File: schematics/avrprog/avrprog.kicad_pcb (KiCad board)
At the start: 2 copper layers, 74.9 x 38.1 mm, 37 parts, among them J1 USB_B, J2 AVR-ISP-10, J3 PROG_PWR, J4 EMCLK, J5 SELF_PROG, U1 FT232RL, U2 ATmega8A-P, Y1 16MHz

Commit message: schematic ...
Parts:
- D8: value PPWRLED -> PWRLED
- moved R10 77.1 mm to (92.7, 57.1), turned to -90 degrees
- moved D7 69.5 mm to (99.4, 67.8), turned to 180 degrees
- moved R11 44.4 mm to (54.6, 87.6), turned to 90 degrees
- moved C1 9.89 mm to (53.3, 67.3)
- moved D8 9.04 mm to (38.1, 74.9), turned to -90 degrees
- moved C4 1.54 mm to (38.2, 69.6)
- moved FB1 1.00 mm to (48.0, 67.3)
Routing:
- net VCC: track 0.00 -> 44.2 mm, vias 0 -> 1
- net GND: track 0.00 -> 38.5 mm
- net Net-(D8-Pad2): track 0.00 -> 20.4 mm
- net Net-(FB1-Pad1): track 0.00 -> 14.0 mm, vias 0 -> 1
- net Net-(D2-Pad1): track 0.00 -> 13.2 mm
- net Net-(D1-Pad1): track 0.00 -> 9.94 mm
- net /RXLED#: track 0.00 -> 7.62 mm
- net /USB_D-: track 0.00 -> 5.08 mm
- net /USB_D+: track 0.00 -> 5.08 mm
- net Net-(C2-Pad2): track 0.00 -> 3.83 mm
- net /TXLED#: track 0.00 -> 3.81 mm
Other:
- board size 74.9 x 38.1 mm -> 76.2 x 38.1 mm

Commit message: schematic ...
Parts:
- added C10: 100nF, Capacitor_THT:C_Disc_D3.8mm_W2.6mm_P2.50mm, F.Cu at (54.6, 77.5)
- moved D8 70.4 mm to (96.5, 35.6)
- moved R11 66.6 mm to (88.9, 30.5), turned to -90 degrees
- moved D7 32.1 mm to (114.3, 39.4)
- moved R10 26.7 mm to (104.1, 33.0)
- moved J2 10.4 mm to (105.8, 67.3), turned to 180 degrees
- moved J5 3.81 mm to (69.8, 90.2)
- moved C4 2.17 mm to (38.2, 71.8)
- moved R7 1.28 mm to (97.8, 73.7)
- moved R8 1.28 mm to (102.9, 73.7)
- moved R9 1.28 mm to (107.9, 73.7)
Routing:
- net GND: track 38.5 -> 90.3 mm
- net VCC: track 44.2 -> 92.5 mm
- net /RXD_AT: track 0.00 -> 30.4 mm, vias 0 -> 1
- net Net-(D8-Pad2): track 20.4 -> 0.00 mm
- net /CTS_AT#: track 0.00 -> 16.0 mm, vias 0 -> 1
- net /RXD_FT232: track 0.00 -> 14.8 mm, vias 0 -> 1
- net /XTAL2_AT: track 0.00 -> 11.9 mm
- net /RESET_AT: track 0.00 -> 11.4 mm
- net /XTAL1_AT: track 0.00 -> 10.8 mm
- net /DTR_FT232#: track 0.00 -> 9.94 mm
- net Net-(D6-Pad2): track 0.00 -> 3.83 mm
- net Net-(D5-Pad2): track 0.00 -> 3.83 mm
- net Net-(D4-Pad2): track 0.00 -> 3.83 mm
- net /EMCLK_AT: track 0.00 -> 3.81 mm

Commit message: schematics completed
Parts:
- moved R11 45.8 mm to (91.4, 76.2), turned to 90 degrees
- moved R10 43.8 mm to (96.5, 76.2), turned to 90 degrees
- moved R6 36.9 mm to (58.4, 101.6)
- moved R4 35.1 mm to (76.2, 101.6)
- moved J5 34.7 mm to (55.9, 58.4)
- moved C1 27.9 mm to (27.9, 78.7), turned to -90 degrees
- moved D7 26.1 mm to (96.5, 58.4), turned to -90 degrees
- moved R5 24.4 mm to (58.4, 96.5)
- moved R9 24.3 mm to (91.4, 91.4), turned to 0 degrees
- moved D8 23.4 mm to (91.4, 58.4)
- moved FB1 20.8 mm to (27.9, 72.7), turned to -90 degrees
- moved J3 19.4 mm to (101.6, 76.2), turned to 180 degrees
- moved C4 17.6 mm to (53.3, 80.7), turned to 90 degrees
- moved R8 17.1 mm to (91.4, 86.4), turned to 0 degrees
- moved D2 16.3 mm to (48.3, 96.5), turned to 0 degrees
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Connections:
- net /RXD_AT renamed /TXD_FT232
- R5 pad 1: /CTS_AT# -> /RTS_FT232#
- U1 pad 11: /CTS_FT232# -> unconnected-(U1-Pad11)
- U1 pad 3: /CTS_AT# -> /RTS_FT232#
- U2 pad 4: /CTS_FT232# -> unconnected-(U2-Pad4)
- U2 pad 5: /CTS_AT# -> unconnected-(U2-Pad5)
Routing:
- net VCC: track 92.5 -> 0.00 mm, vias 1 -> 0
- net GND: track 90.3 -> 0.00 mm
- net /TXD_FT232: track 30.4 -> 0.00 mm, vias 1 -> 0
- net /CTS_AT#: track 16.0 -> 0.00 mm, vias 1 -> 0
- net /RXD_FT232: track 14.8 -> 0.00 mm, vias 1 -> 0
- net Net-(FB1-Pad1): track 14.0 -> 0.00 mm, vias 1 -> 0
- net Net-(D2-Pad1): track 13.2 -> 0.00 mm
- net /XTAL2_AT: track 11.9 -> 0.00 mm
- net /RESET_AT: track 11.4 -> 0.00 mm
- net /XTAL1_AT: track 10.8 -> 0.00 mm
- net Net-(D1-Pad1): track 9.94 -> 0.00 mm
- net /DTR_FT232#: track 9.94 -> 0.00 mm
- net /RXLED#: track 7.62 -> 0.00 mm
- net /USB_D-: track 5.08 -> 0.00 mm
- net /USB_D+: track 5.08 -> 0.00 mm
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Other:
- board size 76.2 x 38.1 mm -> 86.4 x 48.3 mm

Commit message: PCB finished
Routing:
- net GND: track 0.00 -> 198.4 mm, vias 0 -> 5
- net VCC: track 0.00 -> 155.2 mm, vias 0 -> 2
- net /RXD_FT232: track 0.00 -> 69.0 mm
- net /TXD_FT232: track 0.00 -> 57.3 mm, vias 0 -> 4
- net /RED_AT: track 0.00 -> 53.2 mm
- net /MISO_PRG: track 0.00 -> 35.7 mm, vias 0 -> 2
- net /DTR_FT232#: track 0.00 -> 35.5 mm, vias 0 -> 1
- net /SCK_PRG: track 0.00 -> 32.2 mm, vias 0 -> 2
- net /SCK_AT: track 0.00 -> 31.9 mm, vias 0 -> 1
- net /RESET_AT: track 0.00 -> 30.8 mm
- net /MOSI_PRG: track 0.00 -> 28.7 mm, vias 0 -> 2
- net /RST_PRG#: track 0.00 -> 27.6 mm, vias 0 -> 2
- net /YELLOW_AT: track 0.00 -> 27.0 mm
- net /TXLED#: track 0.00 -> 25.5 mm
- net /RXLED#: track 0.00 -> 23.9 mm, vias 0 -> 1
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
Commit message: crystal changed from 16MHz to 14.7456MHz due to USART communication
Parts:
- Y1: value 16MHz -> 14.7456MHz
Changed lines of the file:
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@@
       (effects (font (size 1 1) (thickness 0.15)))
     )
-    (fp_text value "16MHz" (at 2.44 3.525 90) (layer "F.Fab")
+    (fp_text value "14.7456MHz" (at 2.44 3.525 90) (layer "F.Fab")
       (effects (font (size 1 1) (thickness 0.15)))
     )

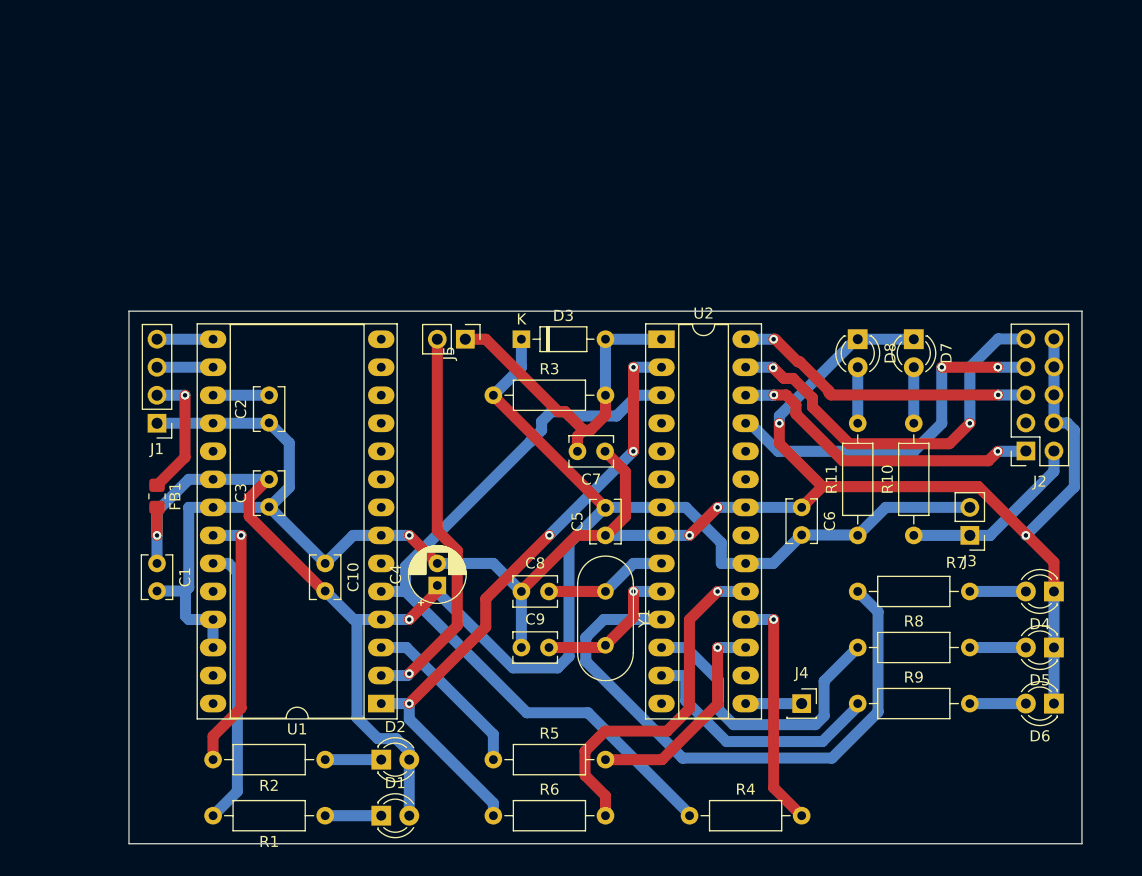
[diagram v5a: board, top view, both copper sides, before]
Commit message: PCB reorganized
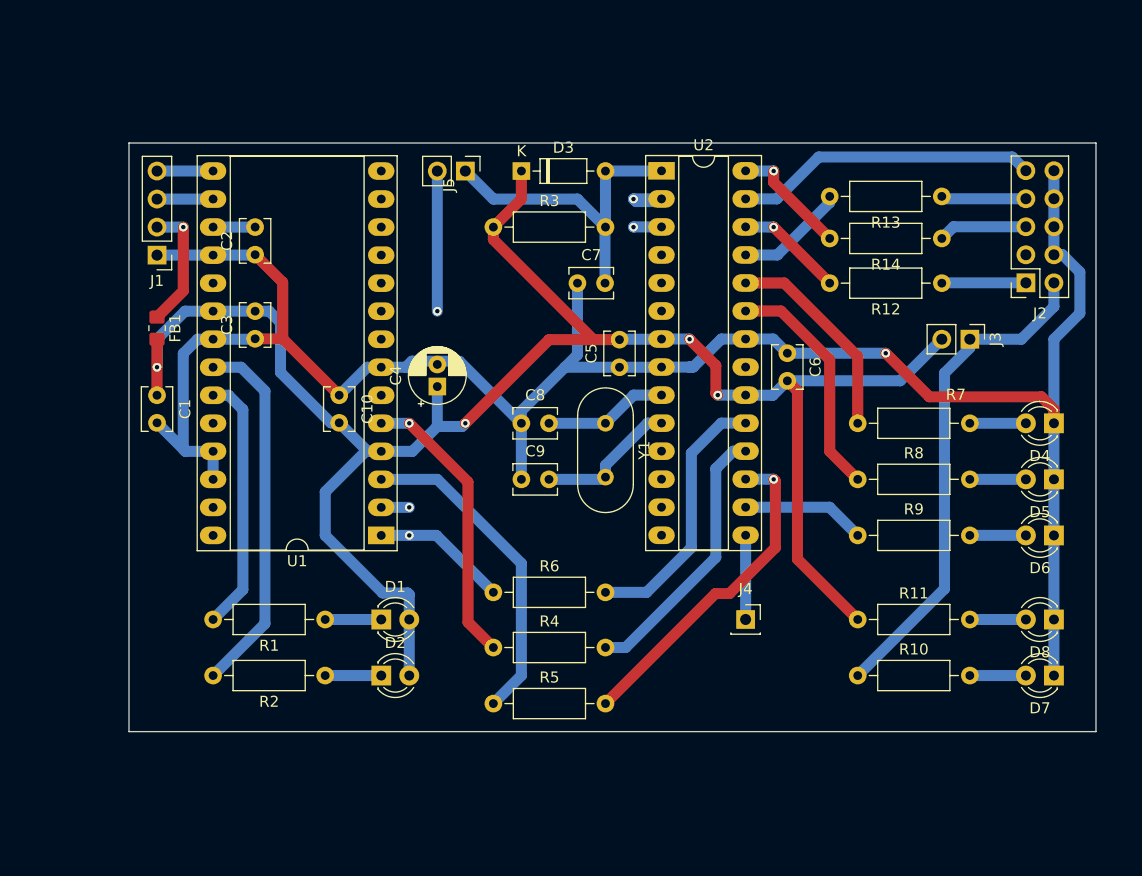
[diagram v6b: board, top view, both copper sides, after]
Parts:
- added R12: 270, Resistor_THT:R_Axial_DIN0207_L6.3mm_D2.5mm_P10.16mm_Horizontal, F.Cu at (99.1, 53.3)
- added R13: 270, Resistor_THT:R_Axial_DIN0207_L6.3mm_D2.5mm_P10.16mm_Horizontal, F.Cu at (99.1, 45.5)
- added R14: 270, Resistor_THT:R_Axial_DIN0207_L6.3mm_D2.5mm_P10.16mm_Horizontal, F.Cu at (99.1, 49.3)
- moved D7 33.0 mm to (109.2, 88.9), turned to 180 degrees
- moved D8 31.0 mm to (109.2, 83.8), turned to 180 degrees
- moved R4 23.4 mm to (58.4, 86.4)
- moved R6 20.2 mm to (58.4, 81.4)
- moved C4 18.0 mm to (53.3, 62.7)
- moved D1 17.8 mm to (48.3, 83.8)
- moved J3 17.8 mm to (101.6, 58.4), turned to -90 degrees
- moved R1 17.8 mm to (43.2, 83.8)
- moved C7 15.4 mm to (66.0, 53.3), turned to 0 degrees
- moved C2 15.3 mm to (36.8, 50.8)
- moved C3 15.3 mm to (36.8, 58.4)
- moved C5 15.3 mm to (69.8, 61.0)
- moved C10 15.3 mm to (44.5, 63.5)
- moved U2 15.3 mm to (73.7, 43.2)
- moved J1 15.2 mm to (27.9, 50.8)
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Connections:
- J2 pad 1: /MOSI_PRG -> Net-(J2-Pad1)
- J2 pad 5: /RST_PRG# -> Net-(J2-Pad5)
- J2 pad 7: /SCK_PRG -> Net-(J2-Pad7)
- U2 pad 11: /RED_AT -> unconnected-(U2-Pad11)
- U2 pad 12: /YELLOW_AT -> unconnected-(U2-Pad12)
- U2 pad 13: /GREEN_AT -> unconnected-(U2-Pad13)
- U2 pad 16: unconnected-(U2-Pad16) -> /GREEN_AT
- U2 pad 23: unconnected-(U2-Pad23) -> /YELLOW_AT
- U2 pad 24: unconnected-(U2-Pad24) -> /RED_AT
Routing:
- net /RXD_FT232: track 69.0 -> 28.6 mm, vias 0 -> 2
- net /TXD_FT232: track 57.3 -> 17.5 mm, vias 4 -> 2
- net /RED_AT: track 53.2 -> 19.0 mm
- net Net-(J2-Pad2): track 17.0 -> 45.7 mm
- net /SCK_PRG: track 32.2 -> 10.1 mm, vias 2 -> 0
- net /DTR_FT232#: track 35.5 -> 15.2 mm, vias 1 -> 2
- net /MOSI_PRG: track 28.7 -> 9.75 mm, vias 2 -> 1
- net VCC: track 155.2 -> 172.9 mm, vias 2 -> 4
- net /RST_PRG#: track 27.6 -> 10.8 mm, vias 2 -> 1
- net /RTS_FT232#: track 15.7 -> 29.6 mm
- net /GREEN_AT: track 22.9 -> 11.2 mm
- net /MOSI_AT: track 19.9 -> 30.1 mm
- net /RXLED#: track 23.9 -> 33.3 mm, vias 1 -> 0
- net GND: track 198.4 -> 189.5 mm, vias 5 -> 1
- net /MISO_PRG: track 35.7 -> 27.5 mm, vias 2 -> 0
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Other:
- board size 86.4 x 48.3 mm -> 87.6 x 53.3 mm

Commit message: simple PCB correction
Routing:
- net /RED_AT: track 19.0 -> 19.5 mm, vias 0 -> 1
- net /YELLOW_AT: track 21.3 -> 21.8 mm, vias 0 -> 1
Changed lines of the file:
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@@
   (segment (start 33.02 88.9) (end 37.72 84.2) (width 1) (layer "B.Cu") (net 27))
   (segment (start 35.56 60.96) (end 33.02 60.96) (width 1) (layer "B.Cu") (net 27))
-  (segment (start 84.776119 53.325) (end 91.44 59.988881) (width 1) (layer "F.Cu") (net 38))
-  (segment (start 91.44 59.988881) (end 91.44 66.04) (width 1) (layer "F.Cu") (net 38))
-  (segment (start 81.28 53.325) (end 84.776119 53.325) (width 1) (layer "F.Cu") (net 38))
-  (segment (start 84.487692 55.865) (end 88.9 60.277308) (width 1) (layer "F.Cu") (net 39))
-  (segment (start 88.9 68.58) (end 91.44 71.12) (width 1) (layer "F.Cu") (net 39))
-  (segment (start 81.28 55.865) (end 84.487692 55.865) (width 1) (layer "F.Cu") (net 39))
-  (segment (start 88.9 60.277308) (end 88.9 68.58) (width 1) (layer "F.Cu") (net 39))
+  (segment (start 91.44 66.04) (end 91.44 59.132692) (width 1) (layer "F.Cu") (net 38))
+  (segment (start 85.647308 53.34) (end 83.82 53.34) (width 1) (layer "F.Cu") (net 38))
+  (segment (start 91.44 59.132692) (end 85.647308 53.34) (width 1) (layer "F.Cu") (net 38))
+  (via (at 83.82 53.34) (size 0.8) (drill 0.4) (layers "F.Cu" "B.Cu") (free) (net 38))
+  (segment (start 83.805 53.325) (end 83.82 53.34) (width 1) (layer "B.Cu") (net 38))
+  (segment (start 81.28 53.325) (end 83.805 53.325) (width 1) (layer "B.Cu") (net 38))
+  (segment (start 85.35888 55.88) (end 83.82 55.88) (width 1) (layer "F.Cu") (net 39))
+  (segment (start 91.44 71.12) (end 87.98 67.66) (width 1) (layer "F.Cu") (net 39))
+  (segment (start 87.98 58.50112) (end 85.35888 55.88) (width 1) (layer "F.Cu") (net 39))
+  (segment (start 87.98 67.66) (end 87.98 58.50112) (width 1) (layer "F.Cu") (net 39))
+  (via (at 83.82 55.88) (size 0.8) (drill 0.4) (layers "F.Cu" "B.Cu") (free) (net 39))
+  (segment (start 81.28 55.865) (end 83.805 55.865) (width 1) (layer "B.Cu") (net 39))
+  (segment (start 83.805 55.865) (end 83.82 55.88) (width 1) (layer "B.Cu") (net 39))
   (segment (start 88.885 73.645) (end 91.44 76.2) (width 1) (layer "B.Cu") (net 40))
   (segment (start 81.28 73.645) (end 88.885 73.645) (width 1) (layer "B.Cu") (net 40))
